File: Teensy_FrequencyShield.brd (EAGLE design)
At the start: 114.3 x 101.6 mm, 22 parts, among them IC9 78L05F

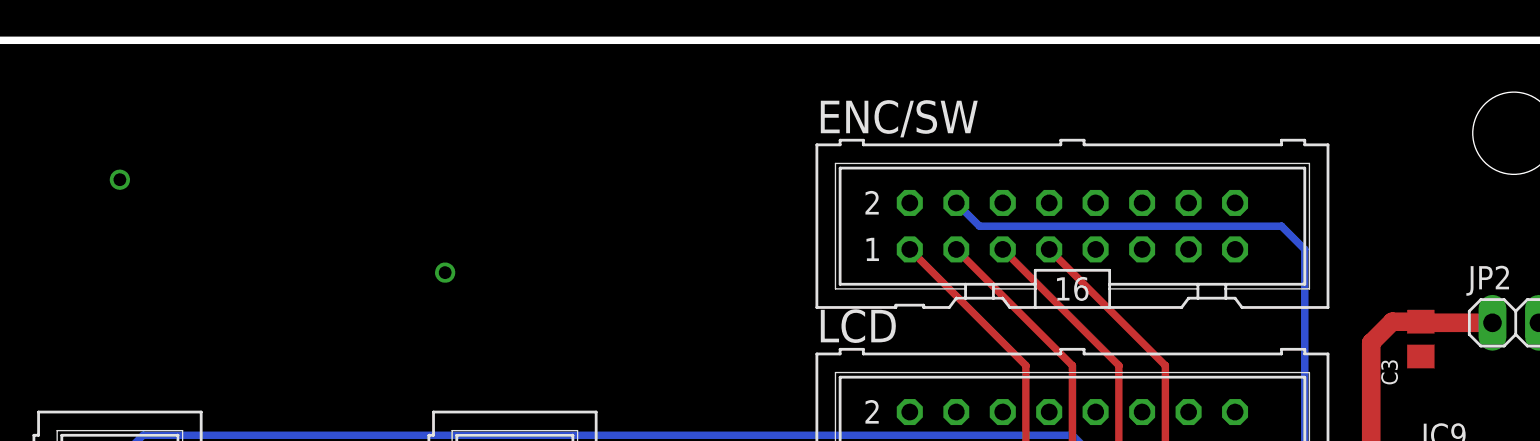
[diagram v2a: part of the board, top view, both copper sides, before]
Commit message: Added optional adjustable Vreg, in case need other voltage.
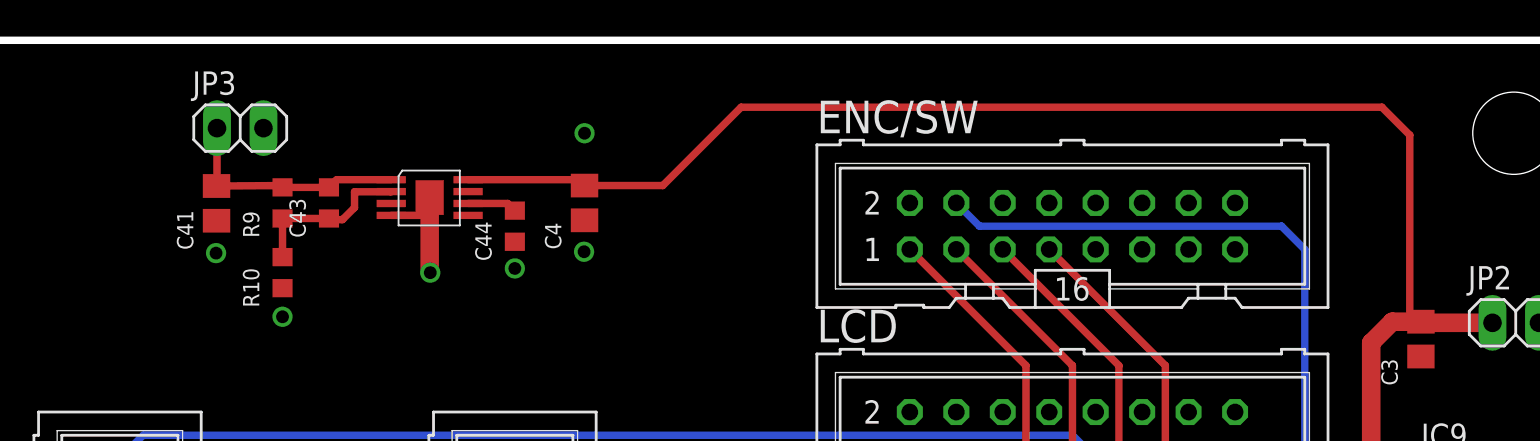
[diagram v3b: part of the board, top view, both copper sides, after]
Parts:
- added C4, C41: 10uF, rlc-jqi:0805
- added C43, C44: 10nF, rlc-jqi:0603
- added JP3: (no value), pinhead:1X02
- added R10, R9: (no value), rlc-jqi:0603
- added U4: TPS7A4901, aom_driver:DGN
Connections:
- new net N$1: C41.2, C43.2, JP3.1, R9.2, U4.OUT
- new net N$49: C43.1, R10.2, R9.1, U4.FB
- new net N$51: C44.2, U4.NR/SS
- net +5V: now also C4.2, U4.IN
- net GND: now also C4.1, C41.1, C44.1, JP3.2, R10.1, U4.GND, U4.GND1
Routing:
- net +5V: track 37.6 -> 101.8 mm
- net N$1: track 0.00 -> 12.9 mm
- net N$49: track 0.00 -> 9.22 mm
- net GND: track 0.00 -> 7.04 mm, vias 18 -> 22
- net N$51: track 0.00 -> 2.72 mm
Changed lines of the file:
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@@
 <?xml version="1.0" encoding="utf-8"?>
 <!DOCTYPE eagle SYSTEM "eagle.dtd">
-<eagle version="6.5.0">
+<eagle version="6.6.0">
 <drawing>
 <settings>
@@
 <setting verticaltext="up"/>
 </settings>
-<grid distance="0.1" unitdist="inch" unit="inch" style="lines" multiple="1" display="yes" altdistance="0.025" altunitdist="inch" altunit="inch"/>
+<grid distance="0.001" unitdist="inch" unit="inch" style="lines" multiple="1" display="yes" altdistance="0.025" altunitdist="inch" altunit="inch"/>
 <layers>
 <layer number="1" name="Top" color="4" fill="1" visible="yes" active="yes"/>
@@
 </element>
 <element name="JP2" library="pinhead" package="1X02" value="" x="2.6416" y="35.3568"/>
+<element name="U4" library="aom_driver" package="DGN" value="TPS7A4901" x="-58.8264" y="43.18" rot="R270">
+<attribute name="PARTNO" value="296-27751-1-ND" x="-51.2064" y="50.8" size="1.778" layer="27" rot="R270" display="off"/>
+</element>
+<element name="C41" library="rlc-jqi" package="0805" value="10uF" x="-68.3768" y="41.8846" rot="R90">
+<attribute name="PARTNO" value="1276-2890-1-ND" x="-68.3768" y="29.1846" size="1.778" layer="27" rot="R90" display="off"/>
+</element>
+<element name="C43" library="rlc-jqi" package="0603" value="10nF" x="-62.23" y="41.91" rot="R90">
+<attribute name="PARTNO" value="1276-1921-1-ND" x="-64.77" y="36.83" size="1.778" layer="27" rot="R90" display="off"/>
+</element>
+<element name="R9" library="rlc-jqi" package="0603" value="" x="-64.77" y="41.91" rot="R90">
+<attribute name="PARTNO" value="P9.10KHCT-ND" x="-67.31" y="36.83" size="1.778" layer="27" rot="R90" display="off"/>
+</element>
+<element name="R10" library="rlc-jqi" package="0603" value="" x="-64.77" y="38.1" rot="R90">
+<attribute name="PARTNO" value="P1.00KHCT-ND" x="-62.23" y="27.94" size="1.778" layer="27" rot="R90" display="off"/>
+</element>
+<element name="C44" library="rlc-jqi" package="0603" value="10nF" x="-52.07" y="40.64" rot="R90">
+<attribute name="PARTNO" value="1276-1921-1-ND" x="-39.37" y="30.48" size="1.778" layer="27" rot="R90" display="off"/>
+</element>
+<element name="C4" library="rlc-jqi" package="0805" value="10uF" x="-48.26" y="41.91" rot="R90">
+<attribute name="PARTNO" value="1276-2890-1-ND" x="-48.26" y="41.91" size="1.778" layer="27" rot="R90" display="off"/>
+</element>
+<element name="JP3" library="pinhead" package="1X02" value="" x="-67.0814" y="45.9994"/>
 </elements>
 <signals>
@@
 <via x="-2.54" y="10.16" extent="1-16" drill="0.7" shape="square"/>
 <via x="17.78" y="22.86" extent="1-16" drill="0.7" shape="square"/>
-<via x="-55.88" y="38.1" extent="1-16" drill="0.7" shape="square"/>
-<via x="-73.66" y="43.18" extent="1-16" drill="0.7" shape="square"/>
+<via x="-56.6928" y="38.1" extent="1-16" drill="0.7" shape="square"/>
+<via x="-48.26" y="45.72" extent="1-16" drill="0.7" shape="square"/>
 <via x="-60.96" y="-5.08" extent="1-16" drill="0.7" shape="square"/>
 <via x="-25.4" y="-38.1" extent="1-16" drill="0.7" shape="square"/>
@@
 <via x="20.32" y="45.72" extent="1-16" drill="0.7" shape="square"/>
 <via x="-5.08" y="20.32" extent="1-16" drill="0.7" shape="square"/>
+<contactref element="U4" pad="GND"/>
+<contactref element="U4" pad="GND1"/>
+<contactref element="R10" pad="1"/>
+<contactref element="C41" pad="1"/>
+<contactref element="C44" pad="1"/>
+<contactref element="C4" pad="1"/>
+<contactref element="JP3" pad="2"/>
+<wire x1="-58.8264" y1="41.23" x2="-56.9918" y2="41.23" width="0.4064" layer="1"/>
+<wire x1="-56.9918" y1="41.23" x2="-56.9214" y2="41.3004" width="0.4064" layer="1"/>
+<wire x1="-56.9214" y1="41.3004" x2="-56.9214" y2="42.01" width="0.4064" layer="1"/>
+<wire x1="-56.9214" y1="42.01" x2="-56.7264" y2="42.205" width="0.4064" layer="1"/>
+<wire x1="-56.7264" y1="42.205" x2="-56.7264" y2="38.1336" width="1.016" layer="1"/>
+<wire x1="-56.7264" y1="38.1336" x2="-56.6928" y2="38.1" width="0.4064" layer="1"/>
 <wire x1="-53.34" y1="-16.51" x2="-50.8" y2="-16.51" width="0" layer="19" extent="1-1"/>
 <wire x1="-53.34" y1="20.32" x2="-53.34" y2="17.78" width="0" layer="19" extent="1-1"/>
@@
 <wire x1="-20.32" y1="-2.54" x2="-12.7" y2="12.7" width="0" layer="19" extent="1-1"/>
 <wire x1="-20.32" y1="-17.78" x2="-20.32" y2="-2.54" width="0" layer="19" extent="1-1"/>
+<via x="-64.77" y="35.687" extent="1-16" drill="0.7" shape="square"/>
+<via x="-52.07" y="38.3286" extent="1-16" drill="0.7" shape="square"/>
+<via x="-48.2854" y="39.243" extent="1-16" drill="0.7" shape="square"/>
+<via x="-68.4022" y="39.1668" extent="1-16" drill="0.7" shape="square"/>
 </signal>
 <signal name="VBAT">
@@
 <wire x1="-5.2578" y1="27.1778" x2="-5.2578" y2="34.2646" width="1.016" layer="1"/>
 <wire x1="-5.2578" y1="34.2646" x2="-4.1046" y2="35.4178" width="1.016" layer="1"/>
-<wire x1="-4.1046" y1="35.4178" x2="-2.54" y2="35.4178" width="1.016" layer="1"/>
+<wire x1="-4.1046" y1="35.4178" x2="-3.1496" y2="35.4178" width="1.016" layer="1"/>
+<contactref element="U4" pad="IN"/>
+<contactref element="C4" pad="2"/>
+<wire x1="-3.1496" y1="35.4178" x2="-2.54" y2="35.4178" width="1.016" layer="1"/>
+<wire x1="-54.6264" y1="43.18" x2="-48.58" y2="43.18" width="0.4064" layer="1"/>
+<wire x1="-48.58" y1="43.18" x2="-48.26" y2="42.86" width="0.4064" layer="1"/>
+<wire x1="-48.26" y1="42.86" x2="-43.9826" y2="42.86" width="0.4064" layer="1"/>
+<wire x1="-43.9826" y1="42.86" x2="-39.7002" y2="47.1424" width="0.4064" layer="1"/>
+<wire x1="-39.7002" y1="47.1424" x2="-4.6736" y2="47.1424" width="0.4064" layer="1"/>
+<wire x1="-4.6736" y1="47.1424" x2="-3.1496" y2="45.6184" width="0.4064" layer="1"/>
+<wire x1="-3.1496" y1="45.6184" x2="-3.1496" y2="35.4178" width="0.4064" layer="1"/>
 </signal>
 <signal name="V+">
@@
 <wire x1="5.4" y1="22.86" x2="5.08" y2="22.54" width="1.016" layer="1"/>
 </signal>
+<signal name="N$49">
+<contactref element="U4" pad="FB"/>
+<contactref element="C43" pad="1"/>
+<contactref element="R10" pad="2"/>
+<contactref element="R9" pad="1"/>
+<wire x1="-64.77" y1="41.06" x2="-62.23" y2="41.06" width="0.4064" layer="1"/>
+<wire x1="-58.8264" y1="42.53" x2="-58.8368" y2="42.5196" width="0.4064" layer="1"/>
+<wire x1="-58.8368" y1="42.5196" x2="-60.833" y2="42.5196" width="0.4064" layer="1"/>
+<wire x1="-60.833" y1="42.5196" x2="-60.833" y2="41.656" width="0.4064" layer="1"/>
+<wire x1="-60.833" y1="41.656" x2="-61.4934" y2="40.9956" width="0.4064" layer="1"/>
+<wire x1="-61.4934" y1="40.9956" x2="-62.1656" y2="40.9956" width="0.4064" layer="1"/>
+<wire x1="-62.1656" y1="40.9956" x2="-62.23" y2="41.06" width="0.4064" layer="1"/>
+<wire x1="-64.77" y1="41.06" x2="-64.77" y2="38.95" width="0.4064" layer="1"/>
+</signal>
+<signal name="N$51">
+<contactref element="C44" pad="2"/>
+<contactref element="U4" pad="NR/SS"/>
+<wire x1="-54.6264" y1="41.88" x2="-52.46" y2="41.88" width="0.4064" layer="1"/>
+<wire x1="-52.46" y1="41.88" x2="-52.07" y2="41.49" width="0.4064" layer="1"/>
+</signal>
+<signal name="N$1">
+<contactref element="U4" pad="OUT"/>
+<contactref element="C43" pad="2"/>
+<contactref element="R9" pad="2"/>
+<contactref element="C41" pad="2"/>
+<contactref element="JP3" pad="1"/>
+<wire x1="-62.23" y1="42.76" x2="-61.81" y2="43.18" width="0.4064" layer="1"/>
+<wire x1="-61.81" y1="43.18" x2="-58.8264" y2="43.18" width="0.4064" layer="1"/>
+<wire x1="-64.77" y1="42.76" x2="-62.23" y2="42.76" width="0.4064" layer="1"/>
+<wire x1="-64.77" y1="42.76" x2="-64.87" y2="42.86" width="0.4064" layer="1"/>
+<wire x1="-64.87" y1="42.86" x2="-68.3768" y2="42.8346" width="0.4064" layer="1"/>
+<wire x1="-68.3514" y1="45.9994" x2="-68.3514" y2="42.86" width="0.4064" layer="1"/>
+<wire x1="-68.3514" y1="42.86" x2="-68.3768" y2="42.8346" width="0.4064" layer="1"/>
+</signal>
 </signals>
